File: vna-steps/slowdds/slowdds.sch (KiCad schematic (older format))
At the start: 9 parts

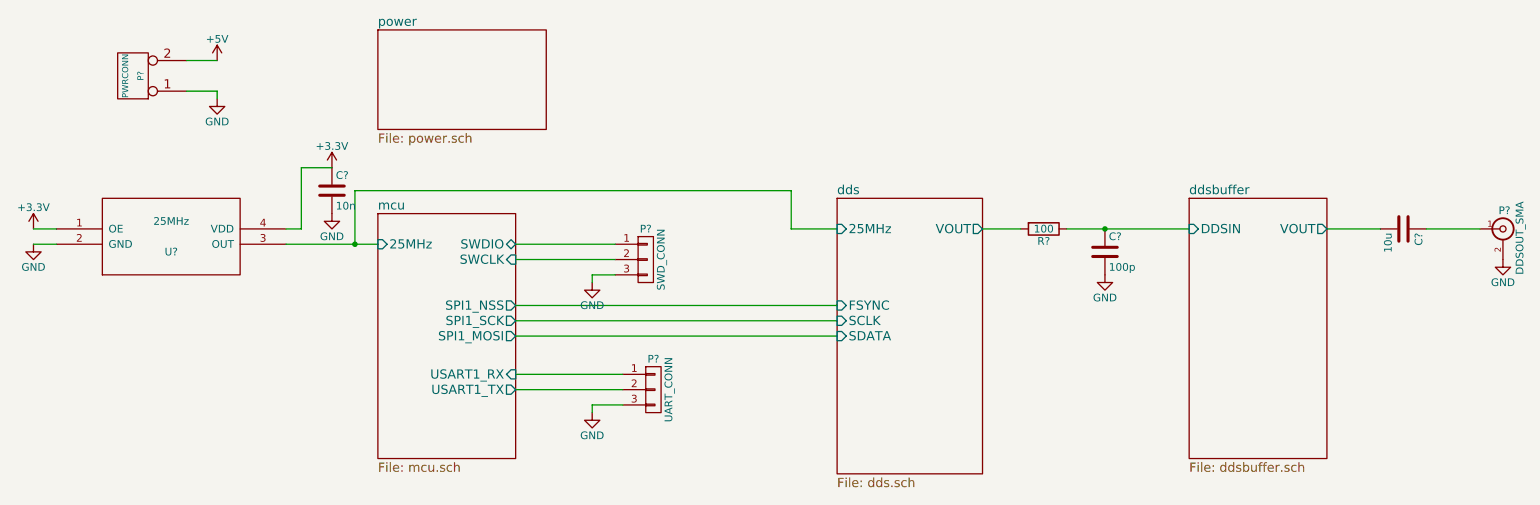
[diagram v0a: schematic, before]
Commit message: slowdds layout completed. images + schematics generated. ZIP file scripts added and documented in README. slowdds gerbers generated + zipped.
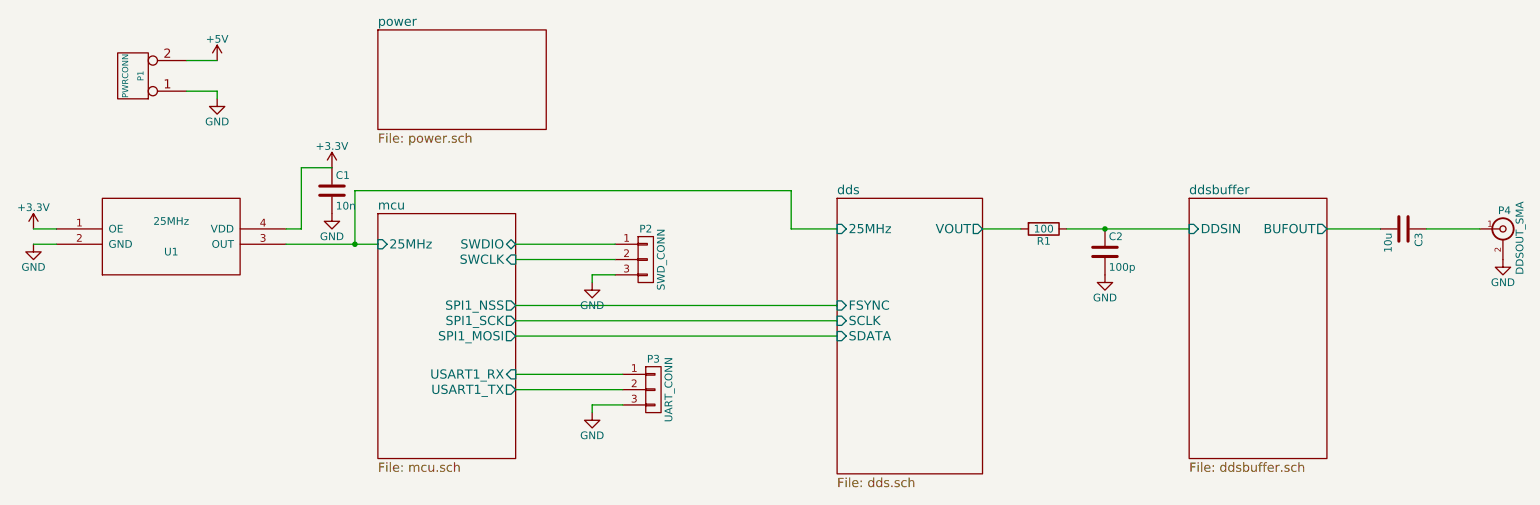
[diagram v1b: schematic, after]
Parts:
- C1: renamed from C?; footprint (none) -> Capacitors_SMD:C_0402
- C2, C3: renamed from C?; footprint (none) -> Capacitors_SMD:C_0603
- P1: renamed from P?; footprint (none) -> Pin_Headers:Pin_Header_Straight_1x02
- P2, P3: renamed from P?; footprint (none) -> Pin_Headers:Pin_Header_Straight_1x03
- P4: renamed from P?; footprint (none) -> w_conn_rf:sma_straight_32k101-400l5
- R1: renamed from R?; footprint (none) -> Resistors_SMD:R_0402
- U1: renamed from U?; footprint MODULE -> bce:SIOSC
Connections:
- net ddsbuffer/VOUT renamed ddsbuffer/BUFOUT
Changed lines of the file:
@@
 encoding utf-8
 Sheet 1 5
-Title ""
-Date ""
-Rev ""
-Comp ""
+Title "VNA-Steps SlowDDS"
+Date "Sat 20 Jun 2015"
+Rev "0.1"
+Comp "Bright Cloud Engineering"
 Comment1 ""
 Comment2 ""
@@
 $EndDescr
 $Comp
-L PWRCONN P?
+L PWRCONN P1
 U 1 1 55851970
 P 1450 1850
-F 0 "P?" V 1400 1850 40  0000 C CNN
+F 0 "P1" V 1400 1850 40  0000 C CNN
 F 1 "PWRCONN" V 1500 1850 40  0000 C CNN
-F 2 "" H 1450 1850 60  0000 C CNN
+F 2 "Pin_Headers:Pin_Header_Straight_1x02" H 1450 1850 60  0001 C CNN
 F 3 "" H 1450 1850 60  0000 C CNN
 	1    1450 1850
@@
 $EndComp
 $Comp
-L GND #PWR?
+L GND #PWR01
 U 1 1 558519E4
 P 2000 2000
-F 0 "#PWR?" H 2000 1750 50  0001 C CNN
+F 0 "#PWR01" H 2000 1750 50  0001 C CNN
 F 1 "GND" H 2000 1850 50  0000 C CNN
 F 2 "" H 2000 2000 60  0000 C CNN
@@
 	2000 1950 2000 2000
 $Comp
-L +5V #PWR?
+L +5V #PWR02
 U 1 1 55851A0D
 P 2000 1750
-F 0 "#PWR?" H 2000 1600 50  0001 C CNN
+F 0 "#PWR02" H 2000 1600 50  0001 C CNN
 F 1 "+5V" H 2000 1890 50  0000 C CNN
 F 2 "" H 2000 1750 60  0000 C CNN
@@
 $EndSheet
 $Comp
-L OSC U?
+L OSC U1
 U 1 1 55853607
 P 1700 2900
-F 0 "U?" H 1700 2800 50  0000 C CNN
+F 0 "U1" H 1700 2800 50  0000 C CNN
 F 1 "25MHz" H 1700 3000 50  0000 C CNN
-F 2 "MODULE" H 1700 2700 50  0001 C CNN
+F 2 "bce:SIOSC" H 1700 2700 50  0001 C CNN
 F 3 "DOCUMENTATION" H 1700 3100 50  0001 C CNN
 	1    1700 2900
@@
 $EndComp
 $Comp
-L +3.3V #PWR?
+L +3.3V #PWR03
 U 1 1 55853772
 P 800 2850
-F 0 "#PWR?" H 800 2700 50  0001 C CNN
+F 0 "#PWR03" H 800 2700 50  0001 C CNN
 F 1 "+3.3V" H 800 2990 50  0000 C CNN
 F 2 "" H 800 2850 60  0000 C CNN
@@
 	800  2850 950  2850
 $Comp
-L GND #PWR?
+L GND #PWR04
 U 1 1 55853846
 P 800 2950
-F 0 "#PWR?" H 800 2700 50  0001 C CNN
+F 0 "#PWR04" H 800 2700 50  0001 C CNN
 F 1 "GND" H 800 2800 50  0000 C CNN
 F 2 "" H 800 2950 60  0000 C CNN
@@
 	2450 2950 3050 2950
 $Comp
-L C C?
+L C C1
 U 1 1 5585397A
 P 2750 2600
-F 0 "C?" H 2775 2700 50  0000 L CNN
+F 0 "C1" H 2775 2700 50  0000 L CNN
 F 1 "10n" H 2775 2500 50  0000 L CNN
-F 2 "" H 2788 2450 30  0000 C CNN
+F 2 "Capacitors_SMD:C_0402" H 2788 2450 30  0001 C CNN
 F 3 "" H 2750 2600 60  0000 C CNN
 	1    2750 2600
@@
 $EndComp
 $Comp
-L GND #PWR?
+L GND #PWR05
 U 1 1 558539B0
 P 2750 2750
-F 0 "#PWR?" H 2750 2500 50  0001 C CNN
+F 0 "#PWR05" H 2750 2500 50  0001 C CNN
 F 1 "GND" H 2750 2600 50  0000 C CNN
 F 2 "" H 2750 2750 60  0000 C CNN
@@
 	2550 2450 2750 2450
 $Comp
-L +3.3V #PWR?
+L +3.3V #PWR06
 U 1 1 55853A68
 P 2750 2450
-F 0 "#PWR?" H 2750 2300 50  0001 C CNN
+F 0 "#PWR06" H 2750 2300 50  0001 C CNN
 F 1 "+3.3V" H 2750 2590 50  0000 C CNN
 F 2 "" H 2750 2450 60  0000 C CNN
@@
 $EndComp
 $Comp
-L CONN_01X03 P?
+L CONN_01X03 P2
 U 1 1 55853DE6
 P 4800 3050
-F 0 "P?" H 4800 3250 50  0000 C CNN
+F 0 "P2" H 4800 3250 50  0000 C CNN
 F 1 "SWD_CONN" V 4900 3050 50  0000 C CNN
-F 2 "" H 4800 3050 60  0000 C CNN
+F 2 "Pin_Headers:Pin_Header_Straight_1x03" H 4800 3050 60  0001 C CNN
 F 3 "" H 4800 3050 60  0000 C CNN
 	1    4800 3050
@@
 	3950 3050 4600 3050
 $Comp
-L GND #PWR?
+L GND #PWR07
 U 1 1 55853FC1
 P 4450 3200
-F 0 "#PWR?" H 4450 2950 50  0001 C CNN
+F 0 "#PWR07" H 4450 2950 50  0001 C CNN
 F 1 "GND" H 4450 3050 50  0000 C CNN
 F 2 "" H 4450 3200 60  0000 C CNN
@@
 	4450 3150 4600 3150
 $Comp
-L CONN_01X03 P?
+L CONN_01X03 P3
 U 1 1 558540FC
 P 4850 3900
-F 0 "P?" H 4850 4100 50  0000 C CNN
+F 0 "P3" H 4850 4100 50  0000 C CNN
 F 1 "UART_CONN" V 4950 3900 50  0000 C CNN
-F 2 "" H 4850 3900 60  0000 C CNN
+F 2 "Pin_Headers:Pin_Header_Straight_1x03" H 4850 3900 60  0001 C CNN
 F 3 "" H 4850 3900 60  0000 C CNN
 	1    4850 3900
@@
 	3950 3900 4650 3900
 $Comp
-L GND #PWR?
+L GND #PWR08
 U 1 1 5585426D
 P 4450 4050
-F 0 "#PWR?" H 4450 3800 50  0001 C CNN
+F 0 "#PWR08" H 4450 3800 50  0001 C CNN
 F 1 "GND" H 4450 3900 50  0000 C CNN
 F 2 "" H 4450 4050 60  0000 C CNN
@@
 Connection ~ 2900 2950
 $Comp
-L R R?
+L R R1
 U 1 1 55855131
 P 7400 2850
-F 0 "R?" V 7480 2850 50  0000 C CNN
+F 0 "R1" V 7480 2850 50  0000 C CNN
 F 1 "100" V 7400 2850 50  0000 C CNN
-F 2 "" V 7330 2850 30  0000 C CNN
+F 2 "Resistors_SMD:R_0402" V 7330 2850 30  0001 C CNN
 F 3 "" H 7400 2850 30  0000 C CNN
 	1    7400 2850
@@
 $EndComp
 $Comp
-L C C?
+L C C2
 U 1 1 558551A5
 P 7800 3000
-F 0 "C?" H 7825 3100 50  0000 L CNN
+F 0 "C2" H 7825 3100 50  0000 L CNN
 F 1 "100p" H 7825 2900 50  0000 L CNN
-F 2 "" H 7838 2850 30  0000 C CNN
+F 2 "Capacitors_SMD:C_0603" H 7838 2850 30  0001 C CNN
 F 3 "" H 7800 3000 60  0000 C CNN
 	1    7800 3000
@@
 	7550 2850 8350 2850
 $Comp
-L GND #PWR?
+L GND #PWR09
 U 1 1 55855343
 P 7800 3150
-F 0 "#PWR?" H 7800 2900 50  0001 C CNN
+F 0 "#PWR09" H 7800 2900 50  0001 C CNN
 F 1 "GND" H 7800 3000 50  0000 C CNN
 F 2 "" H 7800 3150 60  0000 C CNN
@@
 F1 "ddsbuffer.sch" 60
 F2 "DDSIN" I L 8350 2850 60
-F3 "VOUT" O R 9250 2850 60
+F3 "BUFOUT" O R 9250 2850 60
 $EndSheet
 Connection ~ 7800 2850
 $Comp
-L BNC P?
+L BNC P4
 U 1 1 558561A3
 P 10400 2850
-F 0 "P?" H 10410 2970 50  0000 C CNN
+F 0 "P4" H 10410 2970 50  0000 C CNN
 F 1 "DDSOUT_SMA" V 10510 2790 50  0000 C CNN
-F 2 "" H 10400 2850 60  0000 C CNN
+F 2 "w_conn_rf:sma_straight_32k101-400l5" H 10400 2850 60  0001 C CNN
 F 3 "" H 10400 2850 60  0000 C CNN
 	1    10400 2850
@@
 $EndComp
 $Comp
-L GND #PWR?
+L GND #PWR010
 U 1 1 558562FF
 P 10400 3050
-F 0 "#PWR?" H 10400 2800 50  0001 C CNN
+F 0 "#PWR010" H 10400 2800 50  0001 C CNN
 F 1 "GND" H 10400 2900 50  0000 C CNN
 F 2 "" H 10400 3050 60  0000 C CNN
@@
 $EndComp
 $Comp
-L C C?
+L C C3
 U 1 1 558563DC
 P 9750 2850
-F 0 "C?" H 9775 2950 50  0000 L CNN
+F 0 "C3" H 9775 2950 50  0000 L CNN
 F 1 "10u" H 9775 2750 50  0000 L CNN
-F 2 "" H 9788 2700 30  0000 C CNN
+F 2 "Capacitors_SMD:C_0603" H 9788 2700 30  0001 C CNN
 F 3 "" H 9750 2850 60  0000 C CNN
 	1    9750 2850
